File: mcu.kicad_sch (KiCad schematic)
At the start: 16 parts, among them J1 Conn_01x05_Pin, U2 STM32C031C6Tx, U3 M24C02-RMN, Y1 8

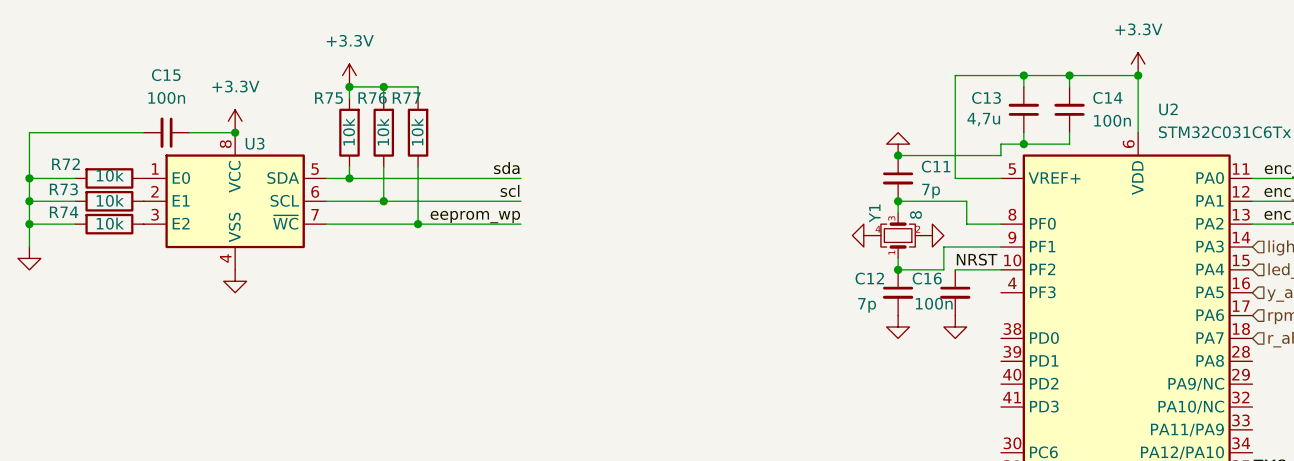
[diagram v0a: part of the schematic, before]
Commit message: Schematic sites change
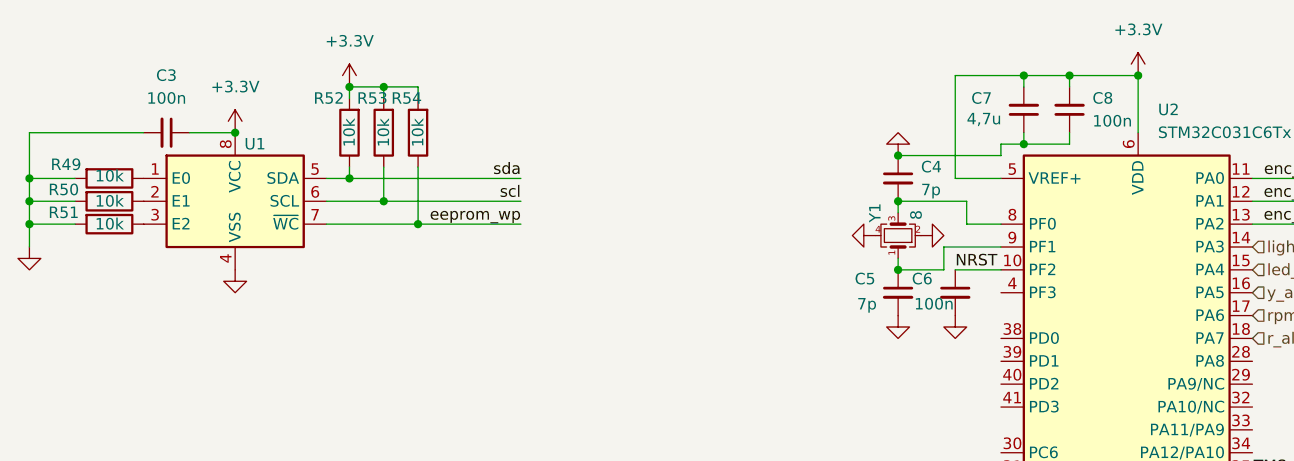
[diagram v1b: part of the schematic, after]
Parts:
- J1: footprint (none) -> Connector_PinHeader_2.54mm:PinHeader_1x05_P2.54mm_Vertical
- renumbered C15 to C3, C11 to C4, C12 to C5, C16 to C6, C13 to C7, C14 to C8, R72 to R49, R73 to R50, R74 to R51, R75 to R52, R76 to R53, R77 to R54, U3 to U1
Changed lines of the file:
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@@
 		(on_board yes)
 		(dnp no)
-		(property "Reference" "C13"
+		(property "Reference" "C7"
 			(at 122.428 29.21 0)
 			(effects
@@
 			(project "rpm_meter"
 				(path "/c95b12ac-441d-4f7a-bd6a-c2e5d81eb286/161f8ec5-4d3d-43af-b95a-56d7e596bfdd"
-					(reference "C13")
+					(reference "C7")
 					(unit 1)
 				)
@@
 		(on_board yes)
 		(dnp no)
-		(property "Reference" "R75"
+		(property "Reference" "R52"
 			(at 51.054 29.21 0)
 			(effects
@@
 			(project "rpm_meter"
 				(path "/c95b12ac-441d-4f7a-bd6a-c2e5d81eb286/161f8ec5-4d3d-43af-b95a-56d7e596bfdd"
-					(reference "R75")
+					(reference "R52")
 					(unit 1)
 				)
@@
 		(on_board yes)
 		(dnp no)
-		(property "Reference" "R77"
+		(property "Reference" "R54"
 			(at 59.69 29.21 0)
 			(effects
@@
 			(project "rpm_meter"
 				(path "/c95b12ac-441d-4f7a-bd6a-c2e5d81eb286/161f8ec5-4d3d-43af-b95a-56d7e596bfdd"
-					(reference "R77")
+					(reference "R54")
 					(unit 1)
 				)
@@
 		(on_board yes)
 		(dnp no)
-		(property "Reference" "R76"
+		(property "Reference" "R53"
 			(at 55.88 29.21 0)
 			(effects
@@
 			(project "rpm_meter"
 				(path "/c95b12ac-441d-4f7a-bd6a-c2e5d81eb286/161f8ec5-4d3d-43af-b95a-56d7e596bfdd"
-					(reference "R76")
+					(reference "R53")
 					(unit 1)
 				)
@@
 		(dnp no)
 		(fields_autoplaced yes)
-		(property "Reference" "#PWR063"
+		(property "Reference" "#PWR033"
 			(at 40.64 54.61 0)
 			(effects
@@
 			(project "rpm_meter"
 				(path "/c95b12ac-441d-4f7a-bd6a-c2e5d81eb286/161f8ec5-4d3d-43af-b95a-56d7e596bfdd"
-					(reference "#PWR063")
+					(reference "#PWR033")
 					(unit 1)
 				)
@@
 		(dnp no)
 		(fields_autoplaced yes)
-		(property "Reference" "#PWR060"
+		(property "Reference" "#PWR041"
 			(at 140.97 133.35 0)
 			(effects
@@
 			(project "rpm_meter"
 				(path "/c95b12ac-441d-4f7a-bd6a-c2e5d81eb286/161f8ec5-4d3d-43af-b95a-56d7e596bfdd"
-					(reference "#PWR060")
+					(reference "#PWR041")
 					(unit 1)
 				)
@@
 		(dnp no)
 		(fields_autoplaced yes)
-		(property "Reference" "C14"
+		(property "Reference" "C8"
 			(at 135.89 29.2035 0)
 			(effects
@@
 			(project "rpm_meter"
 				(path "/c95b12ac-441d-4f7a-bd6a-c2e5d81eb286/161f8ec5-4d3d-43af-b95a-56d7e596bfdd"
-					(reference "C14")
+					(reference "C8")
 					(unit 1)
 				)
@@
 		(dnp no)
 		(fields_autoplaced yes)
-		(property "Reference" "#PWR065"
+		(property "Reference" "#PWR034"
 			(at 53.34 31.75 0)
 			(effects
@@
 			(project "rpm_meter"
 				(path "/c95b12ac-441d-4f7a-bd6a-c2e5d81eb286/161f8ec5-4d3d-43af-b95a-56d7e596bfdd"
-					(reference "#PWR065")
+					(reference "#PWR034")
 					(unit 1)
 				)
@@
 		(dnp no)
 		(fields_autoplaced yes)
-		(property "Reference" "#PWR068"
+		(property "Reference" "#PWR043"
 			(at 243.84 96.52 0)
 			(effects
@@
 			(project "rpm_meter"
 				(path "/c95b12ac-441d-4f7a-bd6a-c2e5d81eb286/161f8ec5-4d3d-43af-b95a-56d7e596bfdd"
-					(reference "#PWR068")
+					(reference "#PWR043")
 					(unit 1)
 				)
@@
 			)
 		)
-		(property "Footprint" ""
+		(property "Footprint" "Connector_PinHeader_2.54mm:PinHeader_1x05_P2.54mm_Vertical"
 			(at 255.27 91.44 0)
 			(effects
@@
 		(on_board yes)
 		(dnp no)
-		(property "Reference" "R73"
+		(property "Reference" "R50"
 			(at 21.59 39.37 90)
 			(effects
@@
 			(project "rpm_meter"
 				(path "/c95b12ac-441d-4f7a-bd6a-c2e5d81eb286/161f8ec5-4d3d-43af-b95a-56d7e596bfdd"
-					(reference "R73")
+					(reference "R50")
 					(unit 1)
 				)
@@
 		(dnp no)
 		(fields_autoplaced yes)
-		(property "Reference" "#PWR064"
+		(property "Reference" "#PWR031"
 			(at 17.78 52.07 0)
 			(effects
@@
 			(project "rpm_meter"
 				(path "/c95b12ac-441d-4f7a-bd6a-c2e5d81eb286/161f8ec5-4d3d-43af-b95a-56d7e596bfdd"
-					(reference "#PWR064")
+					(reference "#PWR031")
 					(unit 1)
 				)
@@
 		(dnp no)
 		(fields_autoplaced yes)
-		(property "Reference" "#PWR062"
+		(property "Reference" "#PWR032"
 			(at 40.64 36.83 0)
 			(effects
@@
 			(project "rpm_meter"
 				(path "/c95b12ac-441d-4f7a-bd6a-c2e5d81eb286/161f8ec5-4d3d-43af-b95a-56d7e596bfdd"
-					(reference "#PWR062")
+					(reference "#PWR032")
 					(unit 1)
 				)
@@
 		(on_board yes)
 		(dnp no)
-		(property "Reference" "R74"
+		(property "Reference" "R51"
 			(at 21.59 41.91 90)
 			(effects
@@
 			(project "rpm_meter"
 				(path "/c95b12ac-441d-4f7a-bd6a-c2e5d81eb286/161f8ec5-4d3d-43af-b95a-56d7e596bfdd"
-					(reference "R74")
+					(reference "R51")
 					(unit 1)
 				)
@@
 		(dnp no)
 		(fields_autoplaced yes)
-		(property "Reference" "#PWR066"
+		(property "Reference" "#PWR039"
 			(at 120.65 59.69 0)
 			(effects
@@
 			(project "rpm_meter"
 				(path "/c95b12ac-441d-4f7a-bd6a-c2e5d81eb286/161f8ec5-4d3d-43af-b95a-56d7e596bfdd"
-					(reference "#PWR066")
+					(reference "#PWR039")
 					(unit 1)
 				)
@@
 		(on_board yes)
 		(dnp no)
-		(property "Reference" "C12"
+		(property "Reference" "C5"
 			(at 109.474 49.276 0)
 			(effects
@@
 			(project "rpm_meter"
 				(path "/c95b12ac-441d-4f7a-bd6a-c2e5d81eb286/161f8ec5-4d3d-43af-b95a-56d7e596bfdd"
-					(reference "C12")
+					(reference "C5")
 					(unit 1)
 				)
@@
 		(dnp no)
 		(fields_autoplaced yes)
-		(property "Reference" "C15"
+		(property "Reference" "C3"
 			(at 33.0136 26.67 90)
 			(effects
@@
 			(project "rpm_meter"
 				(path "/c95b12ac-441d-4f7a-bd6a-c2e5d81eb286/161f8ec5-4d3d-43af-b95a-56d7e596bfdd"
-					(reference "C15")
+					(reference "C3")
 					(unit 1)
 				)
@@
 		(dnp no)
 		(fields_autoplaced yes)
-		(property "Reference" "#PWR059"
+		(property "Reference" "#PWR037"
 			(at 114.3 59.69 0)
 			(effects
@@
 			(project "rpm_meter"
 				(path "/c95b12ac-441d-4f7a-bd6a-c2e5d81eb286/161f8ec5-4d3d-43af-b95a-56d7e596bfdd"
-					(reference "#PWR059")
+					(reference "#PWR037")
 					(unit 1)
 				)
@@
 		(on_board yes)
 		(dnp no)
-		(property "Reference" "C16"
+		(property "Reference" "C6"
 			(at 115.824 49.276 0)
 			(effects
@@
 			(project "rpm_meter"
 				(path "/c95b12ac-441d-4f7a-bd6a-c2e5d81eb286/161f8ec5-4d3d-43af-b95a-56d7e596bfdd"
-					(reference "C16")
+					(reference "C6")
 					(unit 1)
 				)
@@
 		(dnp no)
 		(fields_autoplaced yes)
-		(property "Reference" "#PWR067"
+		(property "Reference" "#PWR042"
 			(at 254 93.98 0)
 			(effects
@@
 			(project "rpm_meter"
 				(path "/c95b12ac-441d-4f7a-bd6a-c2e5d81eb286/161f8ec5-4d3d-43af-b95a-56d7e596bfdd"
-					(reference "#PWR067")
+					(reference "#PWR042")
 					(unit 1)
 				)
@@
 		(on_board yes)
 		(dnp no)
-		(property "Reference" "U3"
+		(property "Reference" "U1"
 			(at 41.656 34.29 0)
 			(effects
@@
 			(project ""
 				(path "/c95b12ac-441d-4f7a-bd6a-c2e5d81eb286/161f8ec5-4d3d-43af-b95a-56d7e596bfdd"
-					(reference "U3")
+					(reference "U1")
 					(unit 1)
 				)
@@
 		(dnp no)
 		(fields_autoplaced yes)
-		(property "Reference" "#PWR056"
+		(property "Reference" "#PWR038"
 			(at 123.19 44.45 0)
 			(effects
@@
 			(project ""
 				(path "/c95b12ac-441d-4f7a-bd6a-c2e5d81eb286/161f8ec5-4d3d-43af-b95a-56d7e596bfdd"
-					(reference "#PWR056")
+					(reference "#PWR038")
 					(unit 1)
 				)
@@
 		(dnp no)
 		(fields_autoplaced yes)
-		(property "Reference" "C11"
+		(property "Reference" "C4"
 			(at 116.84 36.8362 0)
 			(effects
@@
 			(project ""
 				(path "/c95b12ac-441d-4f7a-bd6a-c2e5d81eb286/161f8ec5-4d3d-43af-b95a-56d7e596bfdd"
-					(reference "C11")
+					(reference "C4")
 					(unit 1)
 				)
@@
 		(dnp no)
 		(fields_autoplaced yes)
-		(property "Reference" "#PWR061"
+		(property "Reference" "#PWR040"
 			(at 140.97 30.48 0)
 			(effects
@@
 			(project ""
 				(path "/c95b12ac-441d-4f7a-bd6a-c2e5d81eb286/161f8ec5-4d3d-43af-b95a-56d7e596bfdd"
-					(reference "#PWR061")
+					(reference "#PWR040")
 					(unit 1)
 				)
@@
 		(dnp no)
 		(fields_autoplaced yes)
-		(property "Reference" "#PWR058"
+		(property "Reference" "#PWR036"
 			(at 114.3 29.21 0)
 			(effects
@@
 			(project "rpm_meter"
 				(path "/c95b12ac-441d-4f7a-bd6a-c2e5d81eb286/161f8ec5-4d3d-43af-b95a-56d7e596bfdd"
-					(reference "#PWR058")
+					(reference "#PWR036")
 					(unit 1)
 				)
@@
 		(dnp no)
 		(fields_autoplaced yes)
-		(property "Reference" "#PWR057"
+		(property "Reference" "#PWR035"
 			(at 105.41 44.45 0)
 			(effects
@@
 			(project "rpm_meter"
 				(path "/c95b12ac-441d-4f7a-bd6a-c2e5d81eb286/161f8ec5-4d3d-43af-b95a-56d7e596bfdd"
-					(reference "#PWR057")
+					(reference "#PWR035")
 					(unit 1)
 				)
@@
 		(on_board yes)
 		(dnp no)
-		(property "Reference" "R72"
+		(property "Reference" "R49"
 			(at 21.844 36.576 90)
 			(effects
@@
 			(project "rpm_meter"
 				(path "/c95b12ac-441d-4f7a-bd6a-c2e5d81eb286/161f8ec5-4d3d-43af-b95a-56d7e596bfdd"
-					(reference "R72")
-					(unit 1)
-				)
+					(reference "R49")
+					(unit 1)
+				)

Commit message: Shifting registers
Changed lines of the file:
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@@
-		)
-	)
-	(hierarchical_label "red_led_9"
-		(shape input)
-		(at 245.11 78.74 0)
-		(fields_autoplaced yes)
-		(effects
-			(font
-				(size 1.27 1.27)
-			)
-			(justify left)
 		)
 	)
@@
 		(shape input)
 		(at 153.67 55.88 0)
-		(fields_autoplaced yes)
-		(effects
-			(font
-				(size 1.27 1.27)
-			)
-			(justify left)
-		)
-	)
-	(hierarchical_label "green_led_1"
-		(shape input)
-		(at 245.11 29.21 0)
-		(fields_autoplaced yes)
-		(effects
-			(font
-				(size 1.27 1.27)
-			)
-			(justify left)
-		)
-	)
-	(hierarchical_label "green_led_3"
-		(shape input)
-		(at 245.11 34.29 0)
-		(fields_autoplaced yes)
-		(effects
-			(font
-				(size 1.27 1.27)
-			)
-			(justify left)
-		)
-	)
-	(hierarchical_label "green_led_4"
-		(shape input)
-		(at 245.11 36.83 0)
-		(fields_autoplaced yes)
-		(effects
-			(font
-				(size 1.27 1.27)
-			)
-			(justify left)
-		)
-	)
-	(hierarchical_label "red_led_6"
-		(shape input)
-		(at 245.11 71.12 0)
-		(fields_autoplaced yes)
-		(effects
-			(font
-				(size 1.27 1.27)
-			)
-			(justify left)
-		)
-	)
-	(hierarchical_label "red_led_3"
-		(shape input)
-		(at 245.11 63.5 0)
-		(fields_autoplaced yes)
-		(effects
-			(font
-				(size 1.27 1.27)
-			)
-			(justify left)
-		)
-	)
-	(hierarchical_label "red_led_4"
-		(shape input)
-		(at 245.11 66.04 0)
-		(fields_autoplaced yes)
-		(effects
-			(font
-				(size 1.27 1.27)
-			)
-			(justify left)
-		)
-	)
-	(hierarchical_label "green_led_6"
-		(shape input)
-		(at 245.11 41.91 0)
 		(fields_autoplaced yes)
 		(effects
@@
 		)
 	)
-	(hierarchical_label "red_led_2"
-		(shape input)
-		(at 245.11 60.96 0)
-		(fields_autoplaced yes)
-		(effects
-			(font
-				(size 1.27 1.27)
-			)
-			(justify left)
-		)
-	)
-	(hierarchical_label "red_led_0"
-		(shape input)
-		(at 245.11 55.88 0)
-		(fields_autoplaced yes)
-		(effects
-			(font
-				(size 1.27 1.27)
-			)
-			(justify left)
-		)
-	)
-	(hierarchical_label "red_led_7"
-		(shape input)
-		(at 245.11 73.66 0)
-		(fields_autoplaced yes)
-		(effects
-			(font
-				(size 1.27 1.27)
-			)
-			(justify left)
-		)
-	)
 	(hierarchical_label "led_pwm_out_3v3"
 		(shape input)
 		(at 153.67 48.26 0)
-		(fields_autoplaced yes)
-		(effects
-			(font
-				(size 1.27 1.27)
-			)
-			(justify left)
-		)
-	)
-	(hierarchical_label "green_led_8"
-		(shape input)
-		(at 245.11 46.99 0)
-		(fields_autoplaced yes)
-		(effects
-			(font
-				(size 1.27 1.27)
-			)
-			(justify left)
-		)
-	)
-	(hierarchical_label "green_led_7"
-		(shape input)
-		(at 245.11 44.45 0)
-		(fields_autoplaced yes)
-		(effects
-			(font
-				(size 1.27 1.27)
-			)
-			(justify left)
-		)
-	)
-	(hierarchical_label "green_led_0"
-		(shape input)
-		(at 245.11 26.67 0)
-		(fields_autoplaced yes)
-		(effects
-			(font
-				(size 1.27 1.27)
-			)
-			(justify left)
-		)
-	)
-	(hierarchical_label "green_led_5"
-		(shape input)
-		(at 245.11 39.37 0)
 		(fields_autoplaced yes)
 		(effects
@@
 		(fields_autoplaced yes)
 		(effects
-			(font
-				(size 1.27 1.27)
-			)
-			(justify left)
-		)
-	)
-	(hierarchical_label "red_led_8"
-		(shape input)
-		(at 245.11 76.2 0)
-		(fields_autoplaced yes)
-		(effects
-			(font
-				(size 1.27 1.27)
-			)
-			(justify left)
-		)
-	)
-	(hierarchical_label "red_led_1"
-		(shape input)
-		(at 245.11 58.42 0)
-		(fields_autoplaced yes)
-		(effects
-			(font
-				(size 1.27 1.27)
-			)
-			(justify left)
-		)
-	)
-	(hierarchical_label "red_led_5"
-		(shape input)
-		(at 245.11 68.58 0)
-		(fields_autoplaced yes)
-		(effects
-			(font
-				(size 1.27 1.27)
-			)
-			(justify left)
-		)
-	)
-	(hierarchical_label "green_led_9"
-		(shape input)
-		(at 245.11 49.53 0)
-		(fields_autoplaced yes)
-		(effects
-			(font
-				(size 1.27 1.27)
-			)
-			(justify left)
-		)
-	)
-	(hierarchical_label "green_led_2"
-		(shape input)
-		(at 245.11 31.75 0)
-		(fields_autoplaced yes)
-		(effects

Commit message: New template
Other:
- company: (none) -> STAPsystem
- title: (none) -> RPM meter LED
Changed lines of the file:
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@@
 	(generator_version "8.0")
 	(paper "A4")
+	(title_block
+		(title "RPM meter LED")
+		(date "2024-11-26")
+		(rev "v1.0")
+		(company "STAPsystem")
+	)
 	(junction
 		(at 60.96 43.18)

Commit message: 27112024
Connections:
- net enc_a: now also U2.17 (PA6); no longer U2.11 (PA0)
- net enc_b: now also U2.18 (PA7); no longer U2.12 (PA1)
- net enc_p: now also U2.41 (PD3); no longer U2.13 (PA2)
- net led_pwm_out_3v3: now also U2.39 (PD1); no longer U2.15 (PA4)
- net light_signal: now also U2.13 (PA2); no longer U2.14 (PA3)
- net r_alert_signal: now also U2.12 (PA1); no longer U2.18 (PA7)
- net rpm_signal_mcu: now also U2.15 (PA4); no longer U2.17 (PA6)
- net y_alert_signal: now also U2.11 (PA0); no longer U2.16 (PA5)
- net SPI_MOSI: now reaches U2.44 (PB5)
- net SPI_SCK: now reaches U2.45 (PB6)
- net LATCH_PIN: now reaches U2.46 (PB7)
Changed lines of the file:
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@@
+	(wire
+		(pts
+			(xy 119.38 63.5) (xy 125.73 63.5)
+		)
+		(stroke
+			(width 0)
+			(type default)
+		)
+	)
 	(wire
 		(pts
@@
 	(wire
 		(pts
-			(xy 160.02 43.18) (xy 153.67 43.18)
-		)
-		(stroke
-			(width 0)
-			(type default)
-		)
-	)
-	(wire
-		(pts
 			(xy 53.34 36.83) (xy 53.34 38.1)
 		)
@@
 	(wire
 		(pts
-			(xy 160.02 38.1) (xy 153.67 38.1)
+			(xy 160.02 53.34) (xy 153.67 53.34)
 		)
 		(stroke
@@
 	(wire
 		(pts
+			(xy 160.02 55.88) (xy 153.67 55.88)
+		)
+		(stroke
+			(width 0)
+			(type default)
+		)
+	)
+	(wire
+		(pts
 			(xy 125.73 34.29) (xy 128.27 34.29)
 		)
@@
 	(wire
 		(pts
-			(xy 160.02 40.64) (xy 153.67 40.64)
-		)
-		(stroke
-			(width 0)
-			(type default)
-		)
-	)
-	(wire
-		(pts
 			(xy 128.27 26.67) (xy 133.35 26.67)
 		)
@@
 			(width 0)
 			(type default)
-		)
-	)
-	(label "enc_a"
-		(at 160.02 38.1 180)
-		(fields_autoplaced yes)
-		(effects
-			(font
-				(size 1.27 1.27)
-			)
-			(justify right bottom)
 		)
 	)
@@
 		)
 	)
-	(label "enc_b"
-		(at 160.02 40.64 180)
-		(fields_autoplaced yes)
-		(effects
-			(font
-				(size 1.27 1.27)
-			)
-			(justify right bottom)
-		)
-	)
 	(label "scl"
 		(at 157.48 101.6 180)
@@
 		)
 	)
+	(label "enc_b"
+		(at 160.02 55.88 180)
+		(fields_autoplaced yes)
+		(effects
+			(font
+				(size 1.27 1.27)
+			)
+			(justify right bottom)
+		)
+	)
 	(label "sda"
 		(at 72.39 38.1 180)
@@
 		)
 	)
+	(label "enc_p"
+		(at 119.38 63.5 0)
+		(fields_autoplaced yes)
+		(effects
+			(font
+				(size 1.27 1.27)
+			)
+			(justify left bottom)
+		)
+	)
 	(label "NRST"
 		(at 120.65 48.26 0)
@@
 		)
 	)
+	(label "enc_a"
+		(at 160.02 53.34 180)
+		(fields_autoplaced yes)
+		(effects
+			(font
+				(size 1.27 1.27)
+			)
+			(justify right bottom)
+		)
+	)
 	(label "TMS"
 		(at 157.48 71.12 180)
@@
 		)
 	)
-	(label "enc_p"
-		(at 160.02 43.18 180)
-		(fields_autoplaced yes)
-		(effects
-			(font
-				(size 1.27 1.27)
-			)
-			(justify right bottom)
-		)
-	)
 	(label "TCK"
 		(at 157.48 73.66 180)
@@
 		)
 	)
+	(hierarchical_label "y_alert_signal"
+		(shape input)
+		(at 153.67 38.1 0)
+		(fields_autoplaced yes)
+		(effects
+			(font
+				(size 1.27 1.27)
+			)
+			(justify left)
+		)
+	)
+	(hierarchical_label "LATCH_PIN"
+		(shape input)
+		(at 153.67 99.06 0)
+		(fields_autoplaced yes)
+		(effects
+			(font
+				(size 1.27 1.27)
+			)
+			(justify left)
+		)
+	)
+	(hierarchical_label "light_signal"
+		(shape input)
+		(at 153.67 43.18 0)
+		(fields_autoplaced yes)
+		(effects
+			(font
+				(size 1.27 1.27)
+			)
+			(justify left)
+		)
+	)
+	(hierarchical_label "led_pwm_out_3v3"
+		(shape input)
+		(at 125.73 58.42 180)
+		(fields_autoplaced yes)
+		(effects
+			(font
+				(size 1.27 1.27)
+			)
+			(justify right)
+		)
+	)
+	(hierarchical_label "SPI_MOSI"
+		(shape input)
+		(at 153.67 93.98 0)
+		(fields_autoplaced yes)
+		(effects
+			(font
+				(size 1.27 1.27)
+			)
+			(justify left)
+		)
+	)
 	(hierarchical_label "r_alert_signal"
 		(shape input)
-		(at 153.67 55.88 0)
+		(at 153.67 40.64 0)
 		(fields_autoplaced yes)
 		(effects
@@
 		)
 	)
-	(hierarchical_label "y_alert_signal"
-		(shape input)
-		(at 153.67 50.8 0)
+	(hierarchical_label "rpm_signal_mcu"
+		(shape input)
+		(at 153.67 48.26 0)
 		(fields_autoplaced yes)
 		(effects
@@
 		)
 	)
-	(hierarchical_label "led_pwm_out_3v3"
-		(shape input)
-		(at 153.67 48.26 0)
-		(fields_autoplaced yes)
-		(effects
-			(font
-				(size 1.27 1.27)
-			)
-			(justify left)
-		)
-	)
-	(hierarchical_label "light_signal"
-		(shape input)
-		(at 153.67 45.72 0)
-		(fields_autoplaced yes)
-		(effects
-			(font
-				(size 1.27 1.27)
-			)
-			(justify left)
-		)
-	)
-	(hierarchical_label "rpm_signal_mcu"
-		(shape input)
-		(at 153.67 53.34 0)
-		(fields_autoplaced yes)
-		(effects
+	(hierarchical_label "SPI_SCK"
+		(shape input)
+		(at 153.67 96.52 0)
+		(fields_autoplaced yes)
+		(effects

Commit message: Placed footprints v1.0
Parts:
- removed J1: Conn_01x05_Pin, Connector_PinHeader_2.54mm:PinHeader_1x05_P2.54mm_Vertical, symbol Connector:Conn_01x05_Pin
- removed R49, R50, R51: 10k, Resistor_SMD:R_0603_1608Metric, symbol Device:R
- added J2: Conn_2Rows-05Pins, Connector_PinHeader_2.54mm:PinHeader_2x03_P2.54mm_Vertical, symbol Connector_Generic:Conn_2Rows-05Pins
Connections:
- net +3.3V: now also J2.4 (Pin_4)
- net GND: now also U1.1 (E0), U1.2 (E1), U1.3 (E2), J2.5 (Pin_5)
- net NRST: now also J2.3 (Pin_3)
- net TCK: now also J2.2 (Pin_2)
- net TMS: now also J2.1 (Pin_1)

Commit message: V1.1
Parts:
- J2: now not fitted; now left out of the parts list
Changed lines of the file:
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@@
 		(unit 1)
 		(exclude_from_sim no)
-		(in_bom yes)
+		(in_bom no)
 		(on_board yes)
-		(dnp no)
+		(dnp yes)
 		(fields_autoplaced yes)
 		(property "Reference" "J2"

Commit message: Encoder
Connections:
- net enc_a renamed ENCODER_A
- net enc_b renamed ENCODER_B
- net enc_p renamed ENCODER_BTN
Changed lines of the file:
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@@
+	(wire
+		(pts
+			(xy 260.35 40.64) (xy 266.7 40.64)
+		)
+		(stroke
+			(width 0)
+			(type default)
+		)
+	)
 	(wire
 		(pts
@@
 	(wire
 		(pts
+			(xy 260.35 38.1) (xy 266.7 38.1)
+		)
+		(stroke
+			(width 0)
+			(type default)
+		)
+	)
+	(wire
+		(pts
 			(xy 53.34 38.1) (xy 72.39 38.1)
 		)
@@
 		(pts
 			(xy 60.96 36.83) (xy 60.96 43.18)
+		)
+		(stroke
+			(width 0)
+			(type default)
+		)
+	)
+	(wire
+		(pts
+			(xy 260.35 35.56) (xy 266.7 35.56)
 		)
 		(stroke
@@
 		)
 	)
+	(label "enc_b"
+		(at 260.35 38.1 0)
+		(fields_autoplaced yes)
+		(effects
+			(font
+				(size 1.27 1.27)
+			)
+			(justify left bottom)
+		)
+	)
 	(label "TMS"
 		(at 236.22 78.74 0)
@@
 		)
 	)
+	(label "enc_a"
+		(at 260.35 35.56 0)
+		(fields_autoplaced yes)
+		(effects
+			(font
+				(size 1.27 1.27)
+			)
+			(justify left bottom)
+		)
+	)
 	(label "NRST"
 		(at 120.65 48.26 0)
@@
 		)
 	)
+	(label "enc_p"
+		(at 260.35 40.64 0)
+		(fields_autoplaced yes)
+		(effects
+			(font
+				(size 1.27 1.27)
+			)
+			(justify left bottom)
+		)
+	)
 	(hierarchical_label "y_alert_signal"
 		(shape input)
@@
 		)
 	)
+	(hierarchical_label "ENCODER_A"
+		(shape input)
+		(at 266.7 35.56 0)
+		(fields_autoplaced yes)
+		(effects
+			(font
+				(size 1.27 1.27)
+			)
+			(justify left)
+		)
+	)
+	(hierarchical_label "ENCODER_B"
+		(shape input)
+		(at 266.7 38.1 0)
+		(fields_autoplaced yes)
+		(effects
+			(font
+				(size 1.27 1.27)
+			)
+			(justify left)
+		)
+	)
+	(hierarchical_label "ENCODER_BTN"
+		(shape input)
+		(at 266.7 40.64 0)
+		(fields_autoplaced yes)
+		(effects
+			(font
+				(size 1.27 1.27)
+			)
+			(justify left)
+		)
+	)
